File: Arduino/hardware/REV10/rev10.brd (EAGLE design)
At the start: 88.3 x 55.9 mm, 47 parts, among them IC2 ATMEGA168-AU, Q1 32768Hz, U1 TC1185SMD, U2 ARDUINO

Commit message: corrected date
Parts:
- moved U$1 47.3 mm to (50.2, 10.9)
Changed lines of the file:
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@@
 <attribute name="NAME" x="52.317525" y="31.7511" size="1" layer="26" font="vector" rot="MR0"/>
 </element>
-<element name="U$1" library="ohw-logo" package="OSHW_10X200_NOTEXT" value="" x="90.874165625" y="35.07610625"/>
+<element name="U$1" library="ohw-logo" package="OSHW_10X200_NOTEXT" value="" x="50.234165625" y="10.94610625"/>
 <element name="C12" library="resistor" package="C0603" value="100nF" x="33.7306125" y="31.63630625" smashed="yes" rot="MR0">
 <attribute name="NAME" x="32.1196125" y="31.14830625" size="1" layer="26" font="vector" rot="MR0"/>

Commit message: updates to rev 10
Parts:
- added DQ/D2: (no value), wirepad:2,15/1,0
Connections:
- net D2: now also DQ/D2.1
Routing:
- net GND: track 266.4 -> 3.75 mm, vias 5 -> 0
- net VCC: track 259.2 -> 2.20 mm, vias 5 -> 0
- net SCL: track 138.9 -> 2.05 mm, vias 4 -> 0
- net 5V: track 114.1 -> 0.00 mm, vias 3 -> 0
- net RESET: track 107.3 -> 0.00 mm, vias 2 -> 0
- net SDA: track 103.4 -> 2.04 mm, vias 5 -> 0
- net D2: track 92.2 -> 0.00 mm, vias 2 -> 0
- net LDR: track 82.1 -> 0.00 mm, vias 2 -> 0
- net IO_POWER_UP: track 79.9 -> 0.00 mm, vias 2 -> 0
- net SPI_MOSI: track 70.7 -> 0.00 mm, vias 1 -> 0
- net N$1: track 69.5 -> 0.00 mm, vias 1 -> 0
- net N$5: track 61.1 -> 0.00 mm, vias 1 -> 0
- net SPI_SCK: track 59.8 -> 0.00 mm, vias 3 -> 0
- net SPI_NSS: track 59.1 -> 0.00 mm, vias 1 -> 0
- net SPI_MISO: track 57.5 -> 0.00 mm, vias 1 -> 0
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- added copper zone on layer 16, net GND

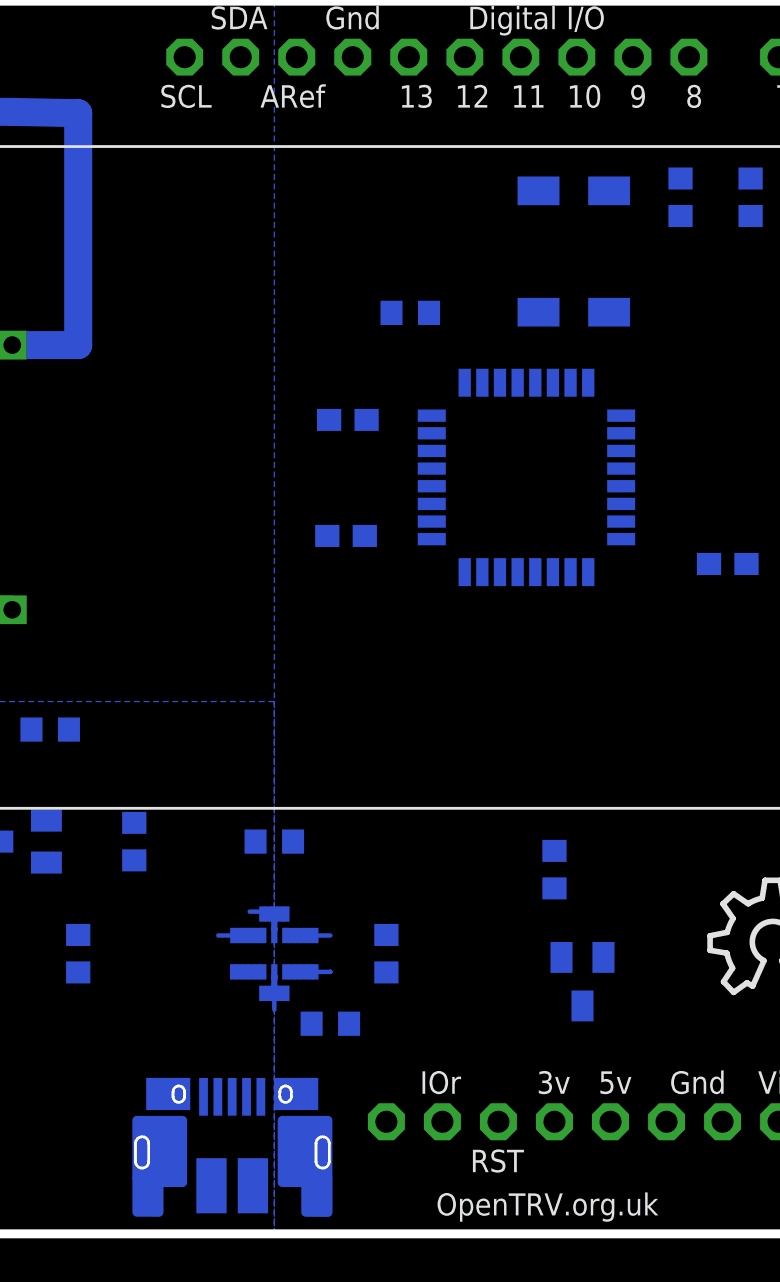
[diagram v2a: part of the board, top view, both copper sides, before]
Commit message: updates to rev 10 & 11
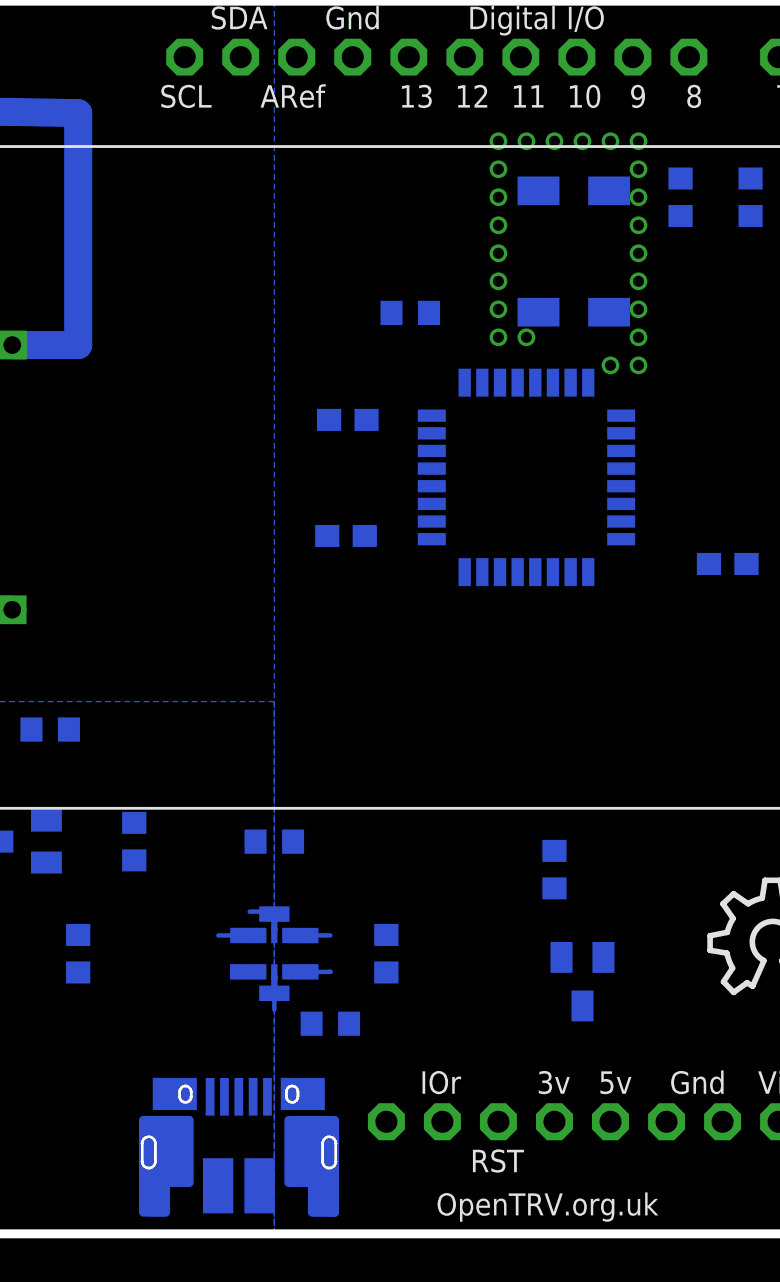
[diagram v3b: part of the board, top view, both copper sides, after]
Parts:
- moved USBPOWER 0.30 mm to (31.4, 3.70)
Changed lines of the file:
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@@
 <attribute name="NAME" x="42.545" y="35.1536" size="1" layer="26" rot="MR270"/>
 </element>
-<element name="USBPOWER" library="micro-usb-fci-10103592" package="MICRO-USB-FCI-10103592" value="MICRO-USB-FCI-10103592" x="31.11" y="3.7" rot="MR0"/>
+<element name="USBPOWER" library="micro-usb-fci-10103592" package="MICRO-USB-FCI-10103592" value="MICRO-USB-FCI-10103592" x="31.41" y="3.7" rot="MR0"/>
 <element name="R6" library="resistor" package="R0603" value="100K" x="33.02" y="9.525" smashed="yes" rot="MR0">
 <attribute name="NAME" x="31.369" y="9.144" size="1" layer="26" rot="MR0"/>
@@
 <wire x1="30.48" y1="11.875" x2="29.98" y2="13.525" width="0" layer="19" extent="16-16"/>
 <wire x1="32.17" y1="9.525" x2="30.48" y2="10.16" width="0" layer="19" extent="16-16"/>
-<wire x1="31.47" y1="6.34" x2="32.17" y2="9.525" width="0" layer="19" extent="16-16"/>
-<wire x1="29.87" y1="6.21" x2="31.47" y2="6.34" width="0" layer="19" extent="16-16"/>
-<wire x1="25.67" y1="6.34" x2="29.87" y2="6.21" width="0" layer="19" extent="16-16"/>
-<wire x1="13.97" y1="6.985" x2="25.67" y2="6.34" width="0" layer="19" extent="16-16"/>
+<wire x1="31.77" y1="6.34" x2="32.17" y2="9.525" width="0" layer="19" extent="16-16"/>
+<wire x1="30.17" y1="6.21" x2="31.77" y2="6.34" width="0" layer="19" extent="16-16"/>
+<wire x1="25.97" y1="6.34" x2="30.17" y2="6.21" width="0" layer="19" extent="16-16"/>
+<wire x1="13.97" y1="6.985" x2="25.97" y2="6.34" width="0" layer="19" extent="16-16"/>
 <wire x1="34.036" y1="53.34" x2="40.71" y2="38.5826" width="0" layer="19" extent="16-16"/>
 <wire x1="48.26" y1="5.08" x2="32.17" y2="9.525" width="0" layer="19" extent="16-16"/>
@@
 <wire x1="52.07" y1="47.84" x2="49.276" y2="53.34" width="0" layer="19" extent="16-16"/>
 </signal>
+<signal name="N$21">
+<via x="40.64" y="46.99" extent="1-16" drill="0.5"/>
+</signal>
+<signal name="N$33">
+<via x="40.64" y="48.26" extent="1-16" drill="0.5"/>
+</signal>
+<signal name="N$34">
+<via x="41.91" y="49.53" extent="1-16" drill="0.5"/>
+</signal>
+<signal name="N$35">
+<via x="40.64" y="49.53" extent="1-16" drill="0.5"/>
+</signal>
+<signal name="N$36">
+<via x="43.18" y="49.53" extent="1-16" drill="0.5"/>
+</signal>
+<signal name="N$37">
+<via x="44.45" y="49.53" extent="1-16" drill="0.5"/>
+</signal>
+<signal name="N$38">
+<via x="45.72" y="49.53" extent="1-16" drill="0.5"/>
+</signal>
+<signal name="N$39">
+<via x="46.99" y="49.53" extent="1-16" drill="0.5"/>
+</signal>
+<signal name="N$40">
+<via x="46.99" y="48.26" extent="1-16" drill="0.5"/>
+</signal>
+<signal name="N$41">
+<via x="46.99" y="46.99" extent="1-16" drill="0.5"/>
+</signal>
+<signal name="N$42">
+<via x="46.99" y="45.72" extent="1-16" drill="0.5"/>
+</signal>
+<signal name="N$43">
+<via x="46.99" y="44.45" extent="1-16" drill="0.5"/>
+</signal>
+<signal name="N$44">
+<via x="46.99" y="43.18" extent="1-16" drill="0.5"/>
+</signal>
+<signal name="N$45">
+<via x="46.99" y="41.91" extent="1-16" drill="0.5"/>
+</signal>
+<signal name="N$46">
+<via x="46.99" y="40.64" extent="1-16" drill="0.5"/>
+</signal>
+<signal name="N$47">
+<via x="46.99" y="39.37" extent="1-16" drill="0.5"/>
+</signal>
+<signal name="N$48">
+<via x="45.72" y="39.37" extent="1-16" drill="0.5"/>
+</signal>
+<signal name="N$49">
+<via x="40.64" y="45.72" extent="1-16" drill="0.5"/>
+</signal>
+<signal name="N$50">
+<via x="40.64" y="44.45" extent="1-16" drill="0.5"/>
+</signal>
+<signal name="N$51">
+<via x="40.64" y="43.18" extent="1-16" drill="0.5"/>
+</signal>
+<signal name="N$52">
+<via x="40.64" y="41.91" extent="1-16" drill="0.5"/>
+</signal>
+<signal name="N$53">
+<via x="40.64" y="40.64" extent="1-16" drill="0.5"/>
+</signal>
+<signal name="N$54">
+<via x="41.91" y="40.64" extent="1-16" drill="0.5"/>
+</signal>
 </signals>

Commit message: bringing things back in sync
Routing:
- net VCC: track 2.20 -> 228.0 mm, vias 0 -> 7
- net SCL: track 2.05 -> 128.2 mm, vias 0 -> 2
- net 5V: track 0.00 -> 115.9 mm, vias 0 -> 2
- net SDA: track 2.04 -> 116.5 mm, vias 0 -> 5
- net D2: track 0.00 -> 102.3 mm, vias 0 -> 1
- net RESET: track 0.00 -> 101.4 mm, vias 0 -> 3
- net LDR: track 0.00 -> 79.4 mm, vias 0 -> 2
- net SPI_MOSI: track 0.00 -> 66.3 mm, vias 0 -> 1
- net SPI_NSS: track 0.00 -> 66.3 mm, vias 0 -> 1
- net SPI_SCK: track 0.00 -> 65.5 mm, vias 0 -> 3
- net SPI_MISO: track 0.00 -> 59.7 mm, vias 0 -> 2
- net IO_POWER_UP: track 0.00 -> 58.0 mm, vias 0 -> 3
- net N$5: track 0.00 -> 56.4 mm
- net LED_HEATCALL_L: track 0.00 -> 55.5 mm
- net VOICE: track 0.00 -> 53.1 mm
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
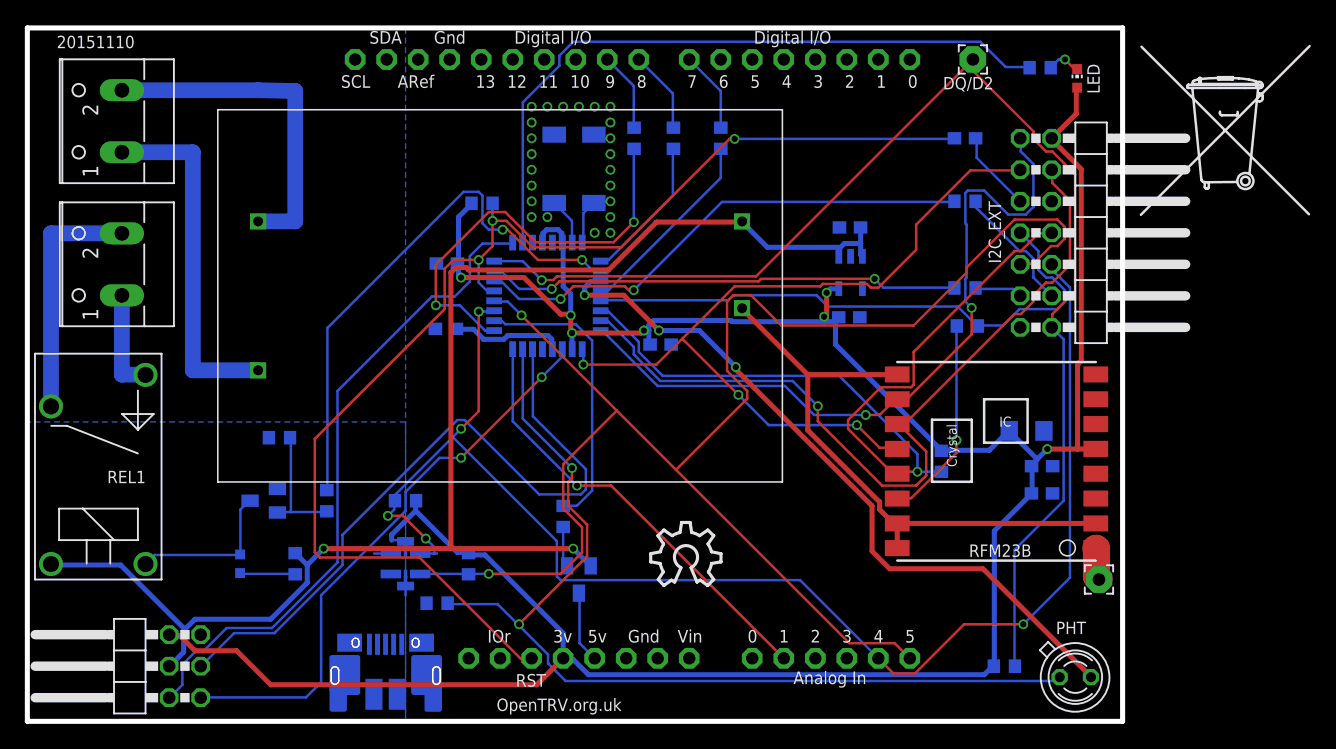
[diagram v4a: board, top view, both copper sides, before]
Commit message: rev10 and rev11 routed again
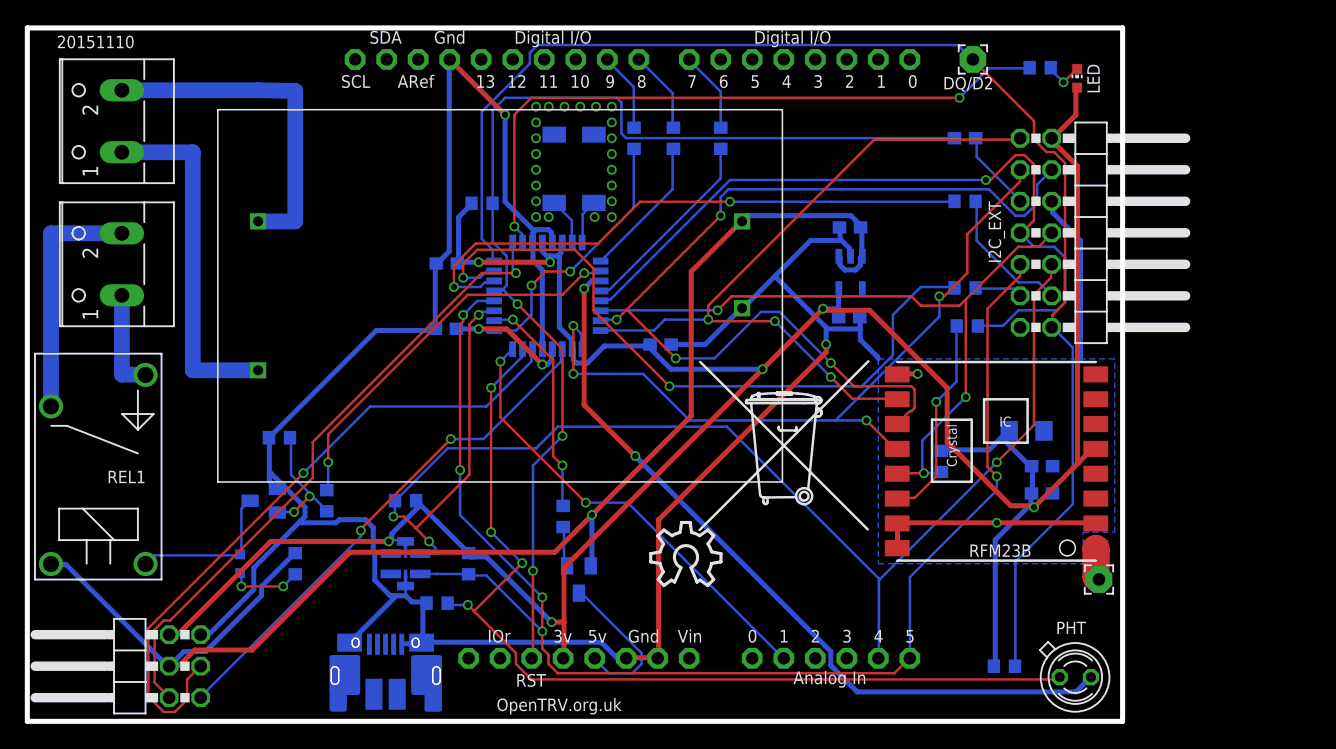
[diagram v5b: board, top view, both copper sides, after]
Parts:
- moved U$2 43.7 mm to (60.8, 19.5)
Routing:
- net GND: track 51.8 -> 238.3 mm, vias 0 -> 4
- net RX: track 38.3 -> 55.7 mm
- net SCL: track 128.2 -> 112.6 mm, vias 2 -> 5
- net RFM_IRQ: track 46.8 -> 62.0 mm, vias 0 -> 1
- net N$11: track 34.1 -> 21.5 mm
- net RESET: track 101.4 -> 89.0 mm
- net BOILER: track 43.6 -> 31.9 mm
- net SPI_MOSI: track 66.3 -> 77.3 mm, vias 1 -> 4
- net D2: track 102.3 -> 110.8 mm, vias 1 -> 0
- net VCC: track 228.0 -> 220.0 mm
- net SPI_NSS: track 66.3 -> 58.7 mm, vias 1 -> 3
- net 5VGSM: track 5.77 -> 12.5 mm
- net TX: track 41.2 -> 47.7 mm
- net PFET: track 23.5 -> 18.3 mm, vias 0 -> 2
- net IO_POWER_UP: track 58.0 -> 62.5 mm, vias 3 -> 2
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
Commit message: rev10 touchup
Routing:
- net GND: track 238.3 -> 324.8 mm, vias 4 -> 3
- net BOILER: track 31.9 -> 65.5 mm
- net RESET: track 89.0 -> 121.5 mm
- net N$11: track 21.5 -> 50.5 mm
- net VCC: track 220.0 -> 247.3 mm
- net IO_POWER_UP: track 62.5 -> 78.2 mm
- net RFM_IRQ: track 62.0 -> 47.3 mm, vias 1 -> 0
- net RX: track 55.7 -> 41.6 mm, vias 2 -> 4
- net 5V: track 115.4 -> 101.8 mm, vias 1 -> 3
- net SDA: track 113.1 -> 122.7 mm
- net SCL: track 112.6 -> 122.1 mm, vias 5 -> 4
- net N$1: track 41.7 -> 50.7 mm, vias 2 -> 3
- net D2: track 110.8 -> 102.0 mm, vias 0 -> 1
- net SPI_MISO: track 58.8 -> 51.5 mm
- net 5VGSM: track 12.5 -> 5.77 mm
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- removed copper zone on layer 16, net GND
